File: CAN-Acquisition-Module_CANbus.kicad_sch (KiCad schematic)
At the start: 2 parts

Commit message: Mid-day backup
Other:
- note added: "Add optional split termination!"
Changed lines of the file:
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@@
     (stroke (width 0) (type default) (color 0 0 0 0))
+  )
+  (text "Add optional split termination!" (at 55.88 76.2 0)
+    (effects (font (size 3 3)) (justify left bottom))
   )
   (label "CAN_L{slash}GRN" (at 57.15 50.8 0)

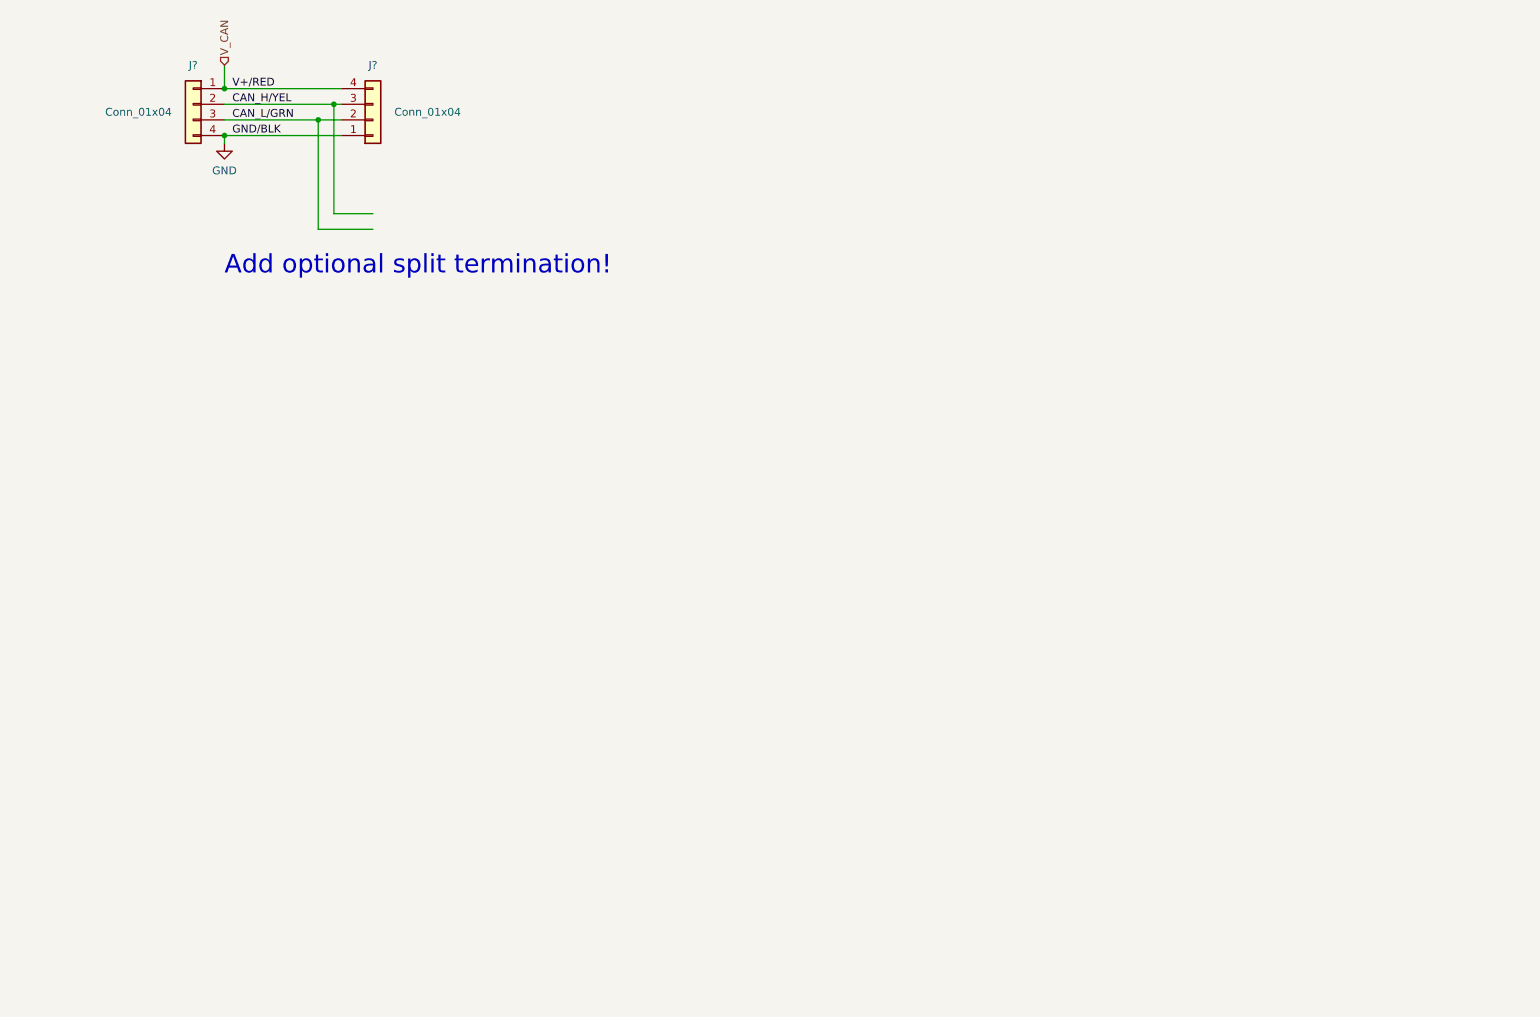
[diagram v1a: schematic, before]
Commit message: Advanced CAN section and "finished" power section
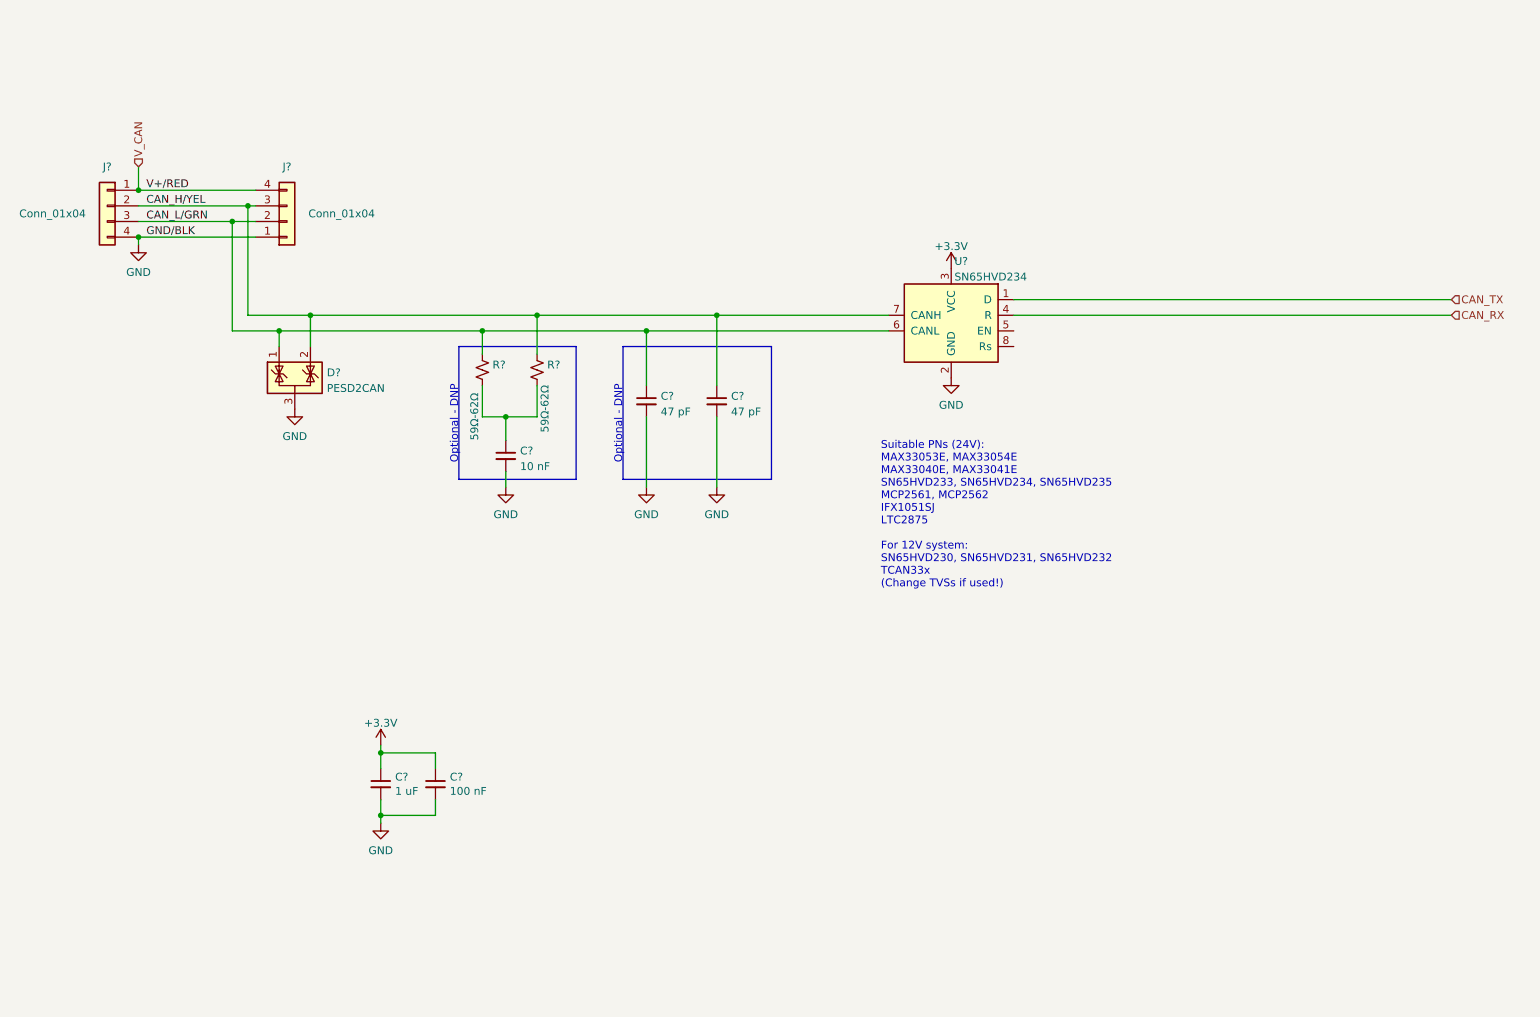
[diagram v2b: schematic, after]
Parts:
- added C? (x2): 47 pF, Capacitor_SMD:C_0603_1608Metric, symbol Device:C_Small
- added C?: 100 nF, Capacitor_SMD:C_0402_1005Metric, symbol Device:C_Small
- added C?: 1 uF, Capacitor_SMD:C_0603_1608Metric, symbol Device:C_Small
- added C?: 10 nF, Capacitor_SMD:C_0603_1608Metric, symbol Device:C_Small
- added D?: PESD2CAN, Package_TO_SOT_SMD:SOT-23, symbol Power_Protection:NUP2105L
- added R? (x2): 59Ω-62Ω, Resistor_SMD:R_1206_3216Metric, symbol Device:R_Small_US
- added U?: SN65HVD234, Package_SO:SOIC-8_3.9x4.9mm_P1.27mm, symbol Interface_CAN_LIN:SN65HVD234
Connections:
- net CAN_H/YEL: now also C?.1, D?.2 (K), R?.1, U?.7 (CANH)
- net CAN_L/GRN: now also C?.1, D?.1 (K), R?.1, U?.6 (CANL)
- net GND: now also C?.2, C?.2, C?.2, C?.2, C?.2, D?.3 (A), U?.2 (GND)
- new net: C?.1, R?.2, R?.2
- new net +3V3: C?.1, C?.1, U?.3 (VCC)
- new net CAN_RX: U?.4 (R)
- new net CAN_TX: U?.1 (D)
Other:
- note added: "Optional - DNP"
- note added: "Suitable PNs (24V): MAX33053E, MAX33054E MAX33040E, MAX33041E SN65HVD233, SN65HVD234, SN65HVD235 MCP2561, MCP2562 IFX1051SJ LTC2875 For 12V system: SN65HVD230, SN65HVD231, SN65HVD232 TCAN33x (Change TVSs if used!)"
- note removed: "Add optional split termination!"
- moved on the sheet: J?

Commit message: Finished CAN section
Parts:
- added C? (x2): F, Capacitor_SMD:C_0603_1608Metric, symbol Device:C_Small
- added R? (x5): Ω, Resistor_SMD:R_0603_1608Metric, symbol Device:R_Small_US
- added R?: 1 kΩ, Resistor_SMD:R_0603_1608Metric, symbol Device:R_Small_US
- added R?: 22 kΩ, Resistor_SMD:R_0603_1608Metric, symbol Device:R_Small_US
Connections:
- net +3V3: now also R?.1, R?.1
- net GND: now also C?.2, C?.2, R?.2, R?.2
- net SPLIT: now reaches C?.1, R?.2, R?.2
- net SPLIT: now also R?.1
- net at U?.5 (EN): now also C?.1, R?.1, R?.1, R?.2, R?.2
- net at U?.8 (Rs): now also C?.1, R?.1, R?.1, R?.2
- new net CAN_PIN5: R?.2
- new net CAN_PIN8: R?.2
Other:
- note added: "Suitable PNs for U?(24V system): MAX33053E, MAX33054E MAX33040E, MAX33041E SN65HVD233, SN65HVD234, SN65HVD235 MCP2561, MCP2562 IFX1051SJ LTC2875 For 12V system: SN65HVD230, SN65HVD231, SN65HVD232 TCAN33x (Change TVSs if used!)"
- note removed: "Suitable PNs (24V): MAX33053E, MAX33054E MAX33040E, MAX33041E SN65HVD233, SN65HVD234, SN65HVD235 MCP2561, MCP2562 IFX1051SJ LTC2875 For 12V system: SN65HVD230, SN65HVD231, SN65HVD232 TCAN33x (Change TVSs if used!)"
- moved on the sheet: C?

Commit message: Added stuff and cleanup
Added LED, Power outputs, additional descriptions
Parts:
- removed J? (x2): Conn_01x04, symbol Connector_Generic:Conn_01x04
- added J? (x2): OSTVN04A150, CAN-Acquisition-Module:OSTVN04A150, symbol Connector:Screw_Terminal_01x04
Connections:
- net CAN_H/YEL: now also J?.2 (Pin_2), J?.3 (Pin_3)
- net CAN_L/GRN: now also J?.2 (Pin_2), J?.3 (Pin_3)
- net GND: now also J?.1 (Pin_1), J?.4 (Pin_4)
- net V_CAN: now also J?.1 (Pin_1), J?.4 (Pin_4)

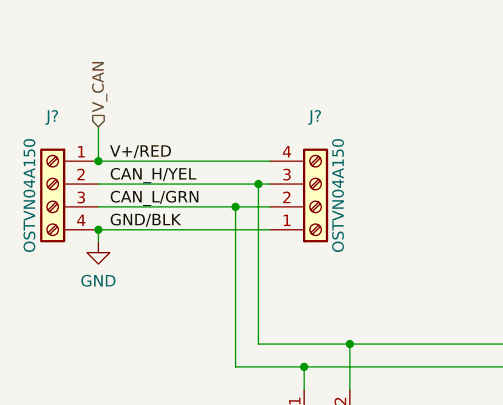
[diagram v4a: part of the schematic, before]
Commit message: Added analog and sensors sections
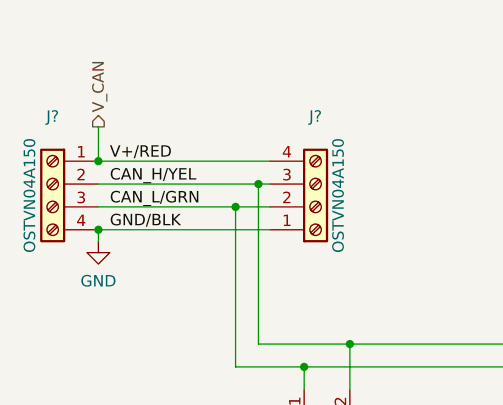
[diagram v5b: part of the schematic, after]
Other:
- company: (none) -> École de Technologie Supérieure - Laboratoire thermique et science du bâtiment (LTSB)
- title: (none) -> CANbus Acquisition Module
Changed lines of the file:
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@@
 (kicad_sch (version 20211123) (generator eeschema)
   (paper "A4")
+  (title_block
+    (title "CANbus Acquisition Module")
+    (date "2022-06-01")
+    (rev "A1")
+    (company "École de Technologie Supérieure - Laboratoire thermique et science du bâtiment (LTSB)")
+    (comment 1 "Designer: Hugo Boyce")
+  )
   (junction (at 208.28 119.38) (diameter 0) (color 0 0 0 0)
   )
@@
     (effects (font (size 1.27 1.27)) (justify left))
   )
-  (hierarchical_label "V_CAN" (shape input) (at 41.91 58.42 90)
+  (hierarchical_label "V_CAN" (shape output) (at 41.91 58.42 90)
     (effects (font (size 1.27 1.27)) (justify left))
   )

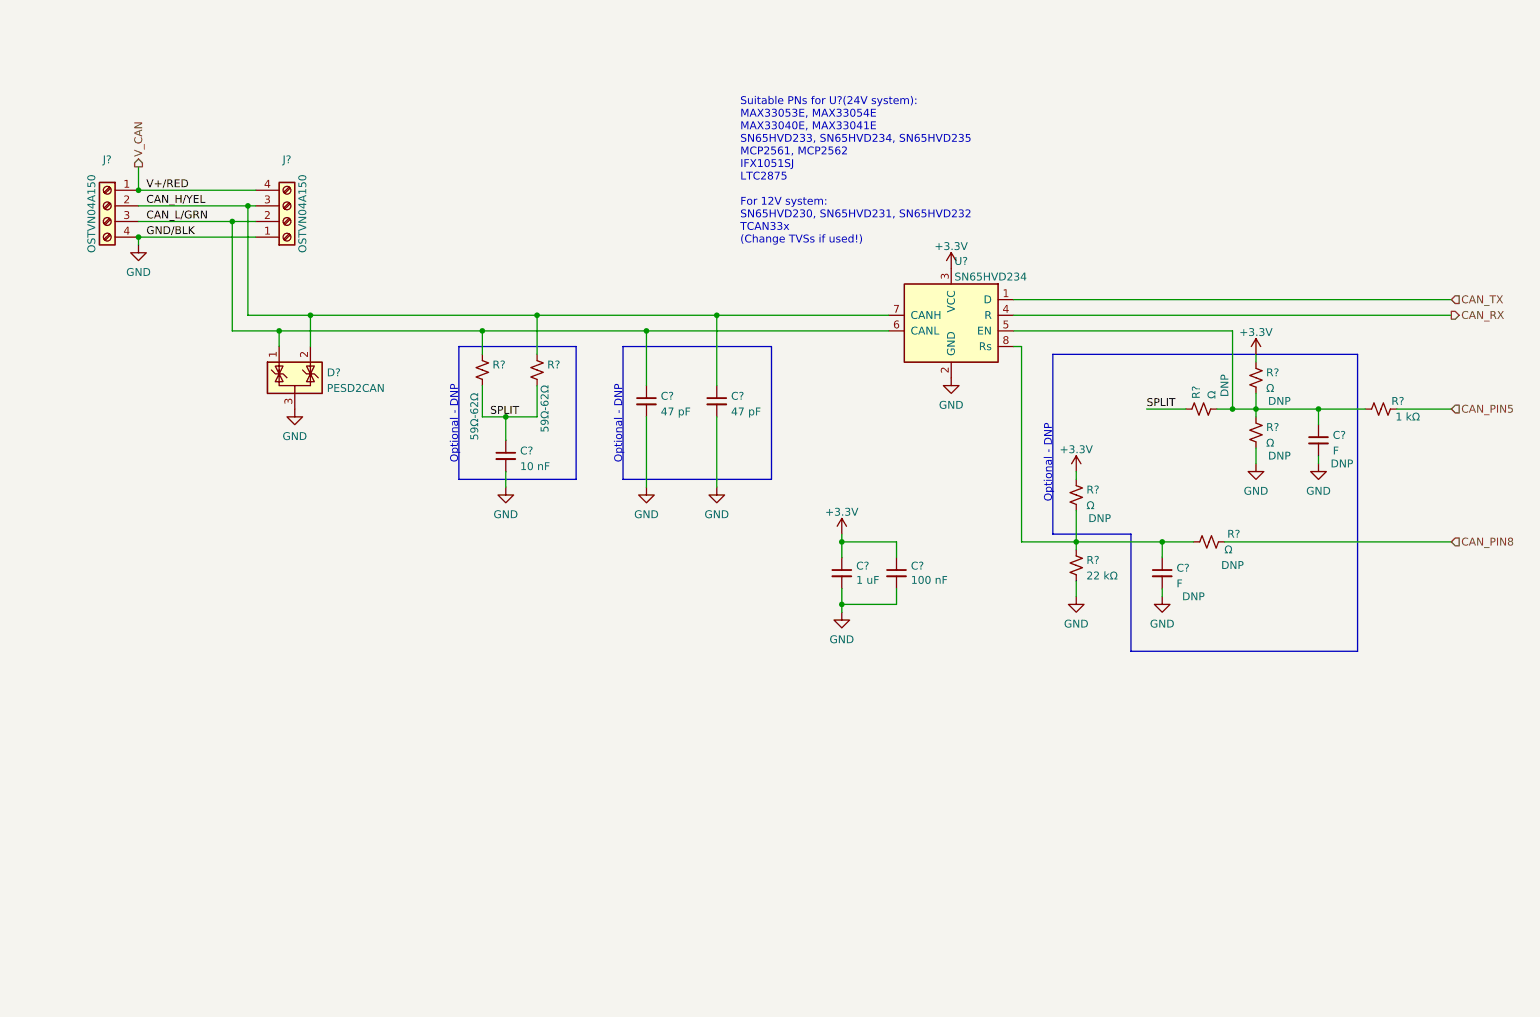
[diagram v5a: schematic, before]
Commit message: Added screen sections and annotations
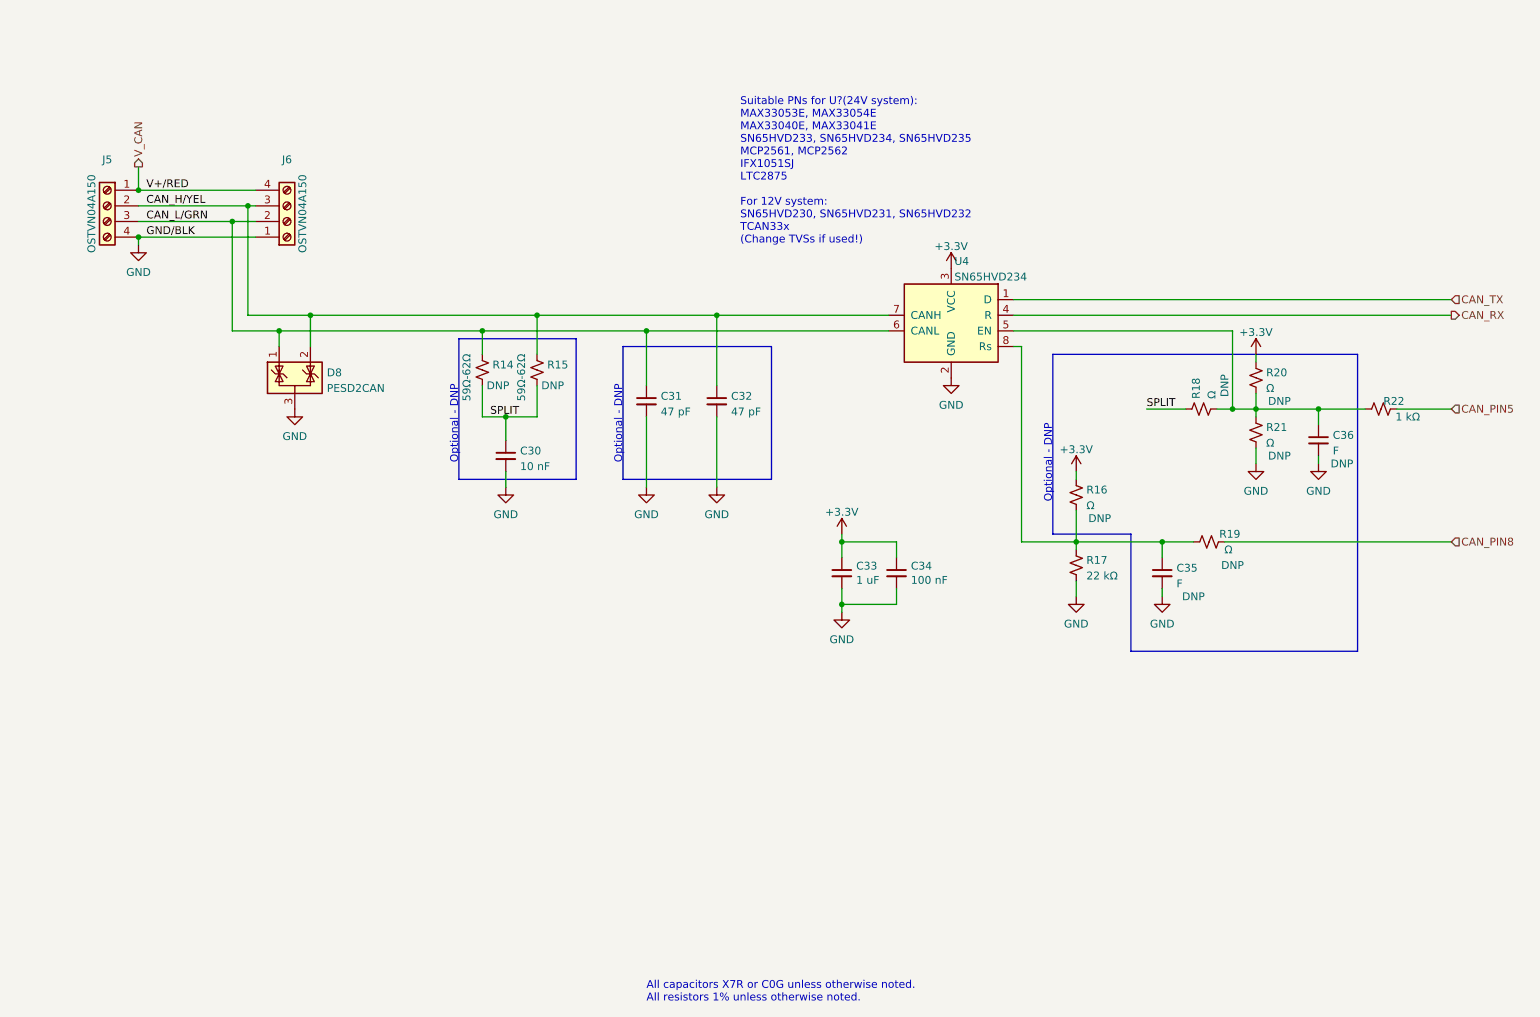
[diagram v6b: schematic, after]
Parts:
- C30: renamed from C?; DNP true -> (none); Do Not Place (none) -> DNP
- C33: renamed from C?; Mfr. (none) -> Samsung Electro-Mechanics; P/N (none) -> CL10B105KA8NNNC; Rated Voltage (none) -> 25V
- C34: renamed from C?; Mfr. (none) -> KYOCERA AVX; P/N (none) -> 0402YC104KAT2A; Rated Voltage (none) -> 16V
- J5, J6: renamed from J?; P/N (none) -> OSTVN04A150
- R14, R15: renamed from R?; DNP true -> (none); Do Not Place (none) -> DNP
- R16, R18, R20: renamed from R?; value Ω -> Ω
- gave numbers to parts that had none: 10
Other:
- note added: "All capacitors X7R or C0G unless otherwise noted. All resistors 1% unless otherwise noted."

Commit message: PCB started
Placement well advanced
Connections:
- net CAN_H/YEL: now also D8.1 (K); no longer D8.2 (K)
- net CAN_L/GRN: now also D8.2 (K); no longer D8.1 (K)
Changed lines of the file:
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@@
   (junction (at 156.21 129.54) (diameter 0) (color 0 0 0 0)
   )
+  (junction (at 69.85 85.09) (diameter 0) (color 0 0 0 0)
+  )
   (junction (at 57.15 67.31) (diameter 0) (color 0 0 0 0)
   )
@@
   (junction (at 194.31 119.38) (diameter 0) (color 0 0 0 0)
   )
-  (junction (at 64.77 85.09) (diameter 0) (color 0 0 0 0)
-  )
-  (junction (at 69.85 82.55) (diameter 0) (color 0 0 0 0)
+  (junction (at 64.77 82.55) (diameter 0) (color 0 0 0 0)
   )
   (junction (at 41.91 69.85) (diameter 0) (color 0 0 0 0)
@@
     (stroke (width 0) (type default) (color 0 0 0 0))
   )
+  (wire (pts (xy 64.77 82.55) (xy 64.77 87.63))
+    (stroke (width 0) (type default) (color 0 0 0 0))
+  )
   (wire (pts (xy 218.44 119.38) (xy 255.27 119.38))
     (stroke (width 0) (type default) (color 0 0 0 0))
@@
     (stroke (width 0) (type default) (color 0 0 0 0))
   )
-  (wire (pts (xy 57.15 85.09) (xy 64.77 85.09))
+  (wire (pts (xy 57.15 85.09) (xy 69.85 85.09))
     (stroke (width 0) (type default) (color 0 0 0 0))
   )
@@
     (stroke (width 0) (type default) (color 0 0 0 0))
   )
-  (wire (pts (xy 69.85 82.55) (xy 69.85 87.63))
-    (stroke (width 0) (type default) (color 0 0 0 0))
-  )
   (wire (pts (xy 223.52 88.9) (xy 223.52 90.17))
     (stroke (width 0) (type default) (color 0 0 0 0))
@@
     (stroke (width 0) (type default) (color 0 0 0 0))
   )
-  (wire (pts (xy 59.69 82.55) (xy 69.85 82.55))
+  (wire (pts (xy 59.69 82.55) (xy 64.77 82.55))
     (stroke (width 0) (type default) (color 0 0 0 0))
   )
@@
     (stroke (width 0) (type default) (color 0 0 0 0))
   )
+  (wire (pts (xy 69.85 85.09) (xy 69.85 87.63))
+    (stroke (width 0) (type default) (color 0 0 0 0))
+  )
   (wire (pts (xy 208.28 121.92) (xy 208.28 119.38))
     (stroke (width 0) (type default) (color 0 0 0 0))
@@
     (stroke (width 0) (type default) (color 0 0 0 0))
   )
+  (wire (pts (xy 69.85 85.09) (xy 97.79 85.09))
+    (stroke (width 0) (type default) (color 0 0 0 0))
+  )
   (wire (pts (xy 106.68 99.06) (xy 101.6 99.06))
     (stroke (width 0) (type default) (color 0 0 0 0))
@@
     (stroke (width 0) (type default) (color 0 0 0 0))
   )
-  (wire (pts (xy 69.85 82.55) (xy 106.68 82.55))
-    (stroke (width 0) (type default) (color 0 0 0 0))
-  )
   (wire (pts (xy 194.31 114.3) (xy 194.31 119.38))
     (stroke (width 0) (type default) (color 0 0 0 0))
@@
     (stroke (width 0) (type default) (color 0 0 0 0))
   )
-  (wire (pts (xy 64.77 85.09) (xy 64.77 87.63))
-    (stroke (width 0) (type default) (color 0 0 0 0))
-  )
   (polyline (pts (xy 144.78 109.22) (xy 120.65 109.22))
     (stroke (width 0) (type default) (color 0 0 0 0))
@@
     (stroke (width 0) (type default) (color 0 0 0 0))
   )
-  (wire (pts (xy 64.77 85.09) (xy 97.79 85.09))
-    (stroke (width 0) (type default) (color 0 0 0 0))
-  )
   (wire (pts (xy 219.71 97.79) (xy 219.71 85.09))
     (stroke (width 0) (type default) (color 0 0 0 0))
@@
     (stroke (width 0) (type default) (color 0 0 0 0))
   )
+  (wire (pts (xy 64.77 82.55) (xy 106.68 82.55))
+    (stroke (width 0) (type default) (color 0 0 0 0))
+  )
